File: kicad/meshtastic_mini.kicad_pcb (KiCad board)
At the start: 2 copper layers, 88 x 84 mm, 128 parts, among them U1 ESP32-C3_SuperMini, U10 RFM95W-868S2, U11 ESP32-C3_SuperMini, U12 RFM95W-868S2, U13 ESP32-C3_SuperMini, U14 RFM95W-868S2, U15 ESP32-C3_SuperMini, U16 RFM95W-868S2, U17 ESP32-C3_SuperMini, U18 RFM95W-868S2, U19 ESP32-C3_SuperMini, U2 RFM95W-868S2, U20 RFM95W-868S2, U21 ESP32-C3_SuperMini, U22 RFM95W-868S2, U23 ESP32-C3_SuperMini, U24 RFM95W-868S2, U25 ESP32-C3_SuperMini, U26 RFM95W-868S2, U27 ESP32-C3_SuperMini, U28 RFM95W-868S2, U29 ESP32-C3_SuperMini, U3 ESP32-C3_SuperMini, U30 RFM95W-868S2, U31 ESP32-C3_SuperMini, U32 RFM95W-868S2, U4 RFM95W-868S2, U5 ESP32-C3_SuperMini, U6 RFM95W-868S2, U7 ESP32-C3_SuperMini, U8 RFM95W-868S2, U9 ESP32-C3_SuperMini

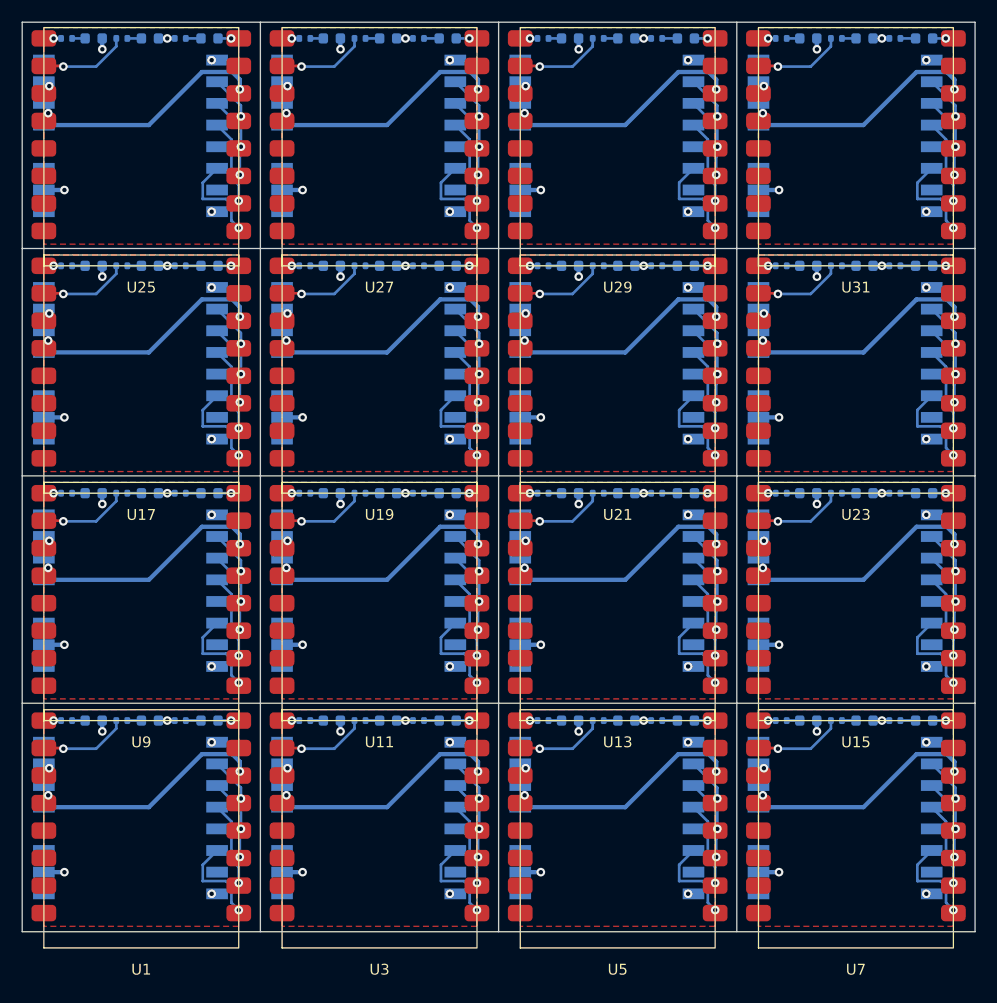
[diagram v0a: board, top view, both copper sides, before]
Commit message: connected DIO0 to pin 10 instead of 9
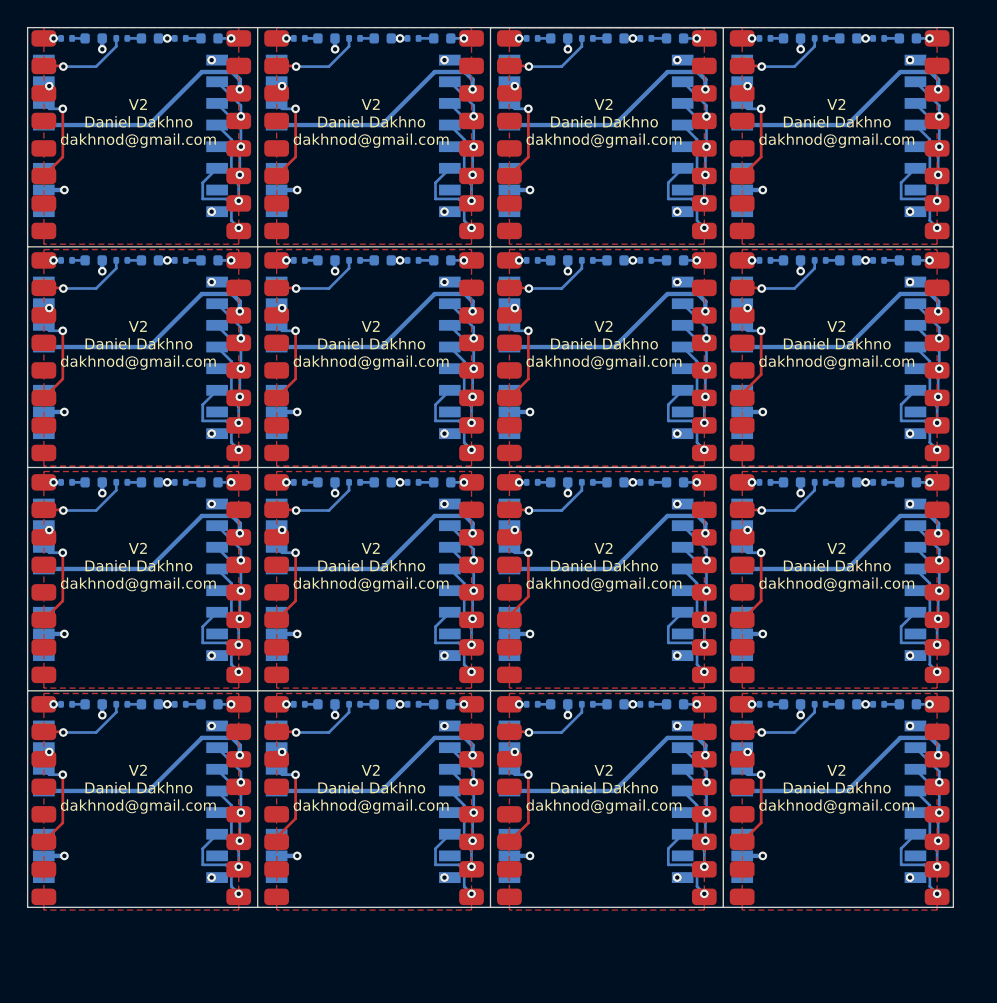
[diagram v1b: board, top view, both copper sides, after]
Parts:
- removed the D1 at (135.6, 103.5)
- removed D10, D11, D12, D13, D14, D15, D16, D17, D18, D19, D20, D21, D22, D23, D24, D25, D26, D27, D28, D29, D30, D31, D32, D33, D34, D35, D36, D4, D40, D41, D42, D43, D44, D45, D46, D47, D48, D5, D6, D7, D8, D9: LED, LED_SMD:LED_0603_1608Metric
- removed the D2 at (140.8, 103.5)
- removed the D3 at (146.3, 103.5)
- removed the R1 at (133.1, 103.5)
- removed R10, R11, R12, R13, R14, R15, R16, R17, R18, R19, R20, R21, R22, R23, R24, R25, R26, R27, R28, R29, R30, R31, R32, R33, R34, R35, R36, R4, R40, R41, R42, R43, R44, R45, R46, R47, R48, R5, R6, R7, R8, R9: 1K, Resistor_SMD:R_0402_1005Metric
- removed the R2 at (138.2, 103.5)
- removed the R3 at (143.6, 103.5)
- removed the U1 at (140.0, 112.5)
- removed U10, U12, U14, U16, U18, U20, U22, U24, U28, U30, U32, U4, U6, U8: RFM95W-868S2, RF_Module:HOPERF_RFM9XW_SMD
- removed U11, U13, U15, U17, U19, U21, U23, U27, U29, U3, U31, U5, U7, U9: ESP32-C3_SuperMini, ESP32:ESP32-C3 SuperMini
- removed the U2 at (139.0, 112.5)
- added D1: LED, LED_SMD:LED_0603_1608Metric, B.Cu at (157.1, 40.5)
- added D1: LED, LED_SMD:LED_0603_1608Metric, B.Cu at (178.6, 61.0)
- added D1: LED, LED_SMD:LED_0603_1608Metric, B.Cu at (200.1, 61.0)
- added D1: LED, LED_SMD:LED_0603_1608Metric, B.Cu at (178.6, 40.5)
- added D1: LED, LED_SMD:LED_0603_1608Metric, B.Cu at (200.1, 40.5)
- added D1: LED, LED_SMD:LED_0603_1608Metric, B.Cu at (135.6, 61.0)
- added D1: LED, LED_SMD:LED_0603_1608Metric, B.Cu at (178.6, 102.0)
- added D1: LED, LED_SMD:LED_0603_1608Metric, B.Cu at (135.6, 81.5)
- added D1: LED, LED_SMD:LED_0603_1608Metric, B.Cu at (178.6, 81.5)
- added D1: LED, LED_SMD:LED_0603_1608Metric, B.Cu at (135.6, 102.0)
- added D1: LED, LED_SMD:LED_0603_1608Metric, B.Cu at (157.1, 61.0)
- added D1: LED, LED_SMD:LED_0603_1608Metric, B.Cu at (157.1, 81.5)
- added D1: LED, LED_SMD:LED_0603_1608Metric, B.Cu at (200.1, 102.0)
- added D1: LED, LED_SMD:LED_0603_1608Metric, B.Cu at (200.1, 81.5)
- added D1: LED, LED_SMD:LED_0603_1608Metric, B.Cu at (157.1, 102.0)
- added D2: LED, LED_SMD:LED_0603_1608Metric, B.Cu at (162.3, 40.5)
- added D2: LED, LED_SMD:LED_0603_1608Metric, B.Cu at (205.3, 81.5)
- added D2: LED, LED_SMD:LED_0603_1608Metric, B.Cu at (140.8, 102.0)
- added D2: LED, LED_SMD:LED_0603_1608Metric, B.Cu at (140.8, 81.5)
- added D2: LED, LED_SMD:LED_0603_1608Metric, B.Cu at (162.3, 81.5)
- added D2: LED, LED_SMD:LED_0603_1608Metric, B.Cu at (183.8, 102.0)
- added D2: LED, LED_SMD:LED_0603_1608Metric, B.Cu at (183.8, 40.5)
- added D2: LED, LED_SMD:LED_0603_1608Metric, B.Cu at (205.3, 40.5)
- added D2: LED, LED_SMD:LED_0603_1608Metric, B.Cu at (183.8, 81.5)
- added D2: LED, LED_SMD:LED_0603_1608Metric, B.Cu at (162.3, 61.0)
- added D2: LED, LED_SMD:LED_0603_1608Metric, B.Cu at (140.8, 61.0)
- added D2: LED, LED_SMD:LED_0603_1608Metric, B.Cu at (205.3, 61.0)
- added D2: LED, LED_SMD:LED_0603_1608Metric, B.Cu at (205.3, 102.0)
- added D2: LED, LED_SMD:LED_0603_1608Metric, B.Cu at (162.3, 102.0)
- added D2: LED, LED_SMD:LED_0603_1608Metric, B.Cu at (183.8, 61.0)
- added D3: LED, LED_SMD:LED_0603_1608Metric, B.Cu at (167.8, 61.0)
- added D3: LED, LED_SMD:LED_0603_1608Metric, B.Cu at (210.8, 40.5)
- added D3: LED, LED_SMD:LED_0603_1608Metric, B.Cu at (210.8, 81.5)
- added D3: LED, LED_SMD:LED_0603_1608Metric, B.Cu at (167.8, 102.0)
- added D3: LED, LED_SMD:LED_0603_1608Metric, B.Cu at (167.8, 40.5)
- added D3: LED, LED_SMD:LED_0603_1608Metric, B.Cu at (189.3, 40.5)
- added D3: LED, LED_SMD:LED_0603_1608Metric, B.Cu at (189.3, 102.0)
- added D3: LED, LED_SMD:LED_0603_1608Metric, B.Cu at (146.3, 81.5)
- added D3: LED, LED_SMD:LED_0603_1608Metric, B.Cu at (189.3, 81.5)
- added D3: LED, LED_SMD:LED_0603_1608Metric, B.Cu at (189.3, 61.0)
- added D3: LED, LED_SMD:LED_0603_1608Metric, B.Cu at (146.3, 102.0)
- added D3: LED, LED_SMD:LED_0603_1608Metric, B.Cu at (210.8, 61.0)
- added D3: LED, LED_SMD:LED_0603_1608Metric, B.Cu at (167.8, 81.5)
- added D3: LED, LED_SMD:LED_0603_1608Metric, B.Cu at (146.3, 61.0)
- added D3: LED, LED_SMD:LED_0603_1608Metric, B.Cu at (210.8, 102.0)
- added R1: 1K, Resistor_SMD:R_0402_1005Metric, B.Cu at (176.1, 81.5)
- added R1: 1K, Resistor_SMD:R_0402_1005Metric, B.Cu at (197.6, 81.5)
- added R1: 1K, Resistor_SMD:R_0402_1005Metric, B.Cu at (133.1, 81.5)
- added R1: 1K, Resistor_SMD:R_0402_1005Metric, B.Cu at (176.1, 61.0)
- added R1: 1K, Resistor_SMD:R_0402_1005Metric, B.Cu at (197.6, 61.0)
- added R1: 1K, Resistor_SMD:R_0402_1005Metric, B.Cu at (197.6, 102.0)
- added R1: 1K, Resistor_SMD:R_0402_1005Metric, B.Cu at (154.6, 102.0)
- added R1: 1K, Resistor_SMD:R_0402_1005Metric, B.Cu at (154.6, 61.0)
- added R1: 1K, Resistor_SMD:R_0402_1005Metric, B.Cu at (197.6, 40.5)
- added R1: 1K, Resistor_SMD:R_0402_1005Metric, B.Cu at (176.1, 40.5)
- added R1: 1K, Resistor_SMD:R_0402_1005Metric, B.Cu at (133.1, 102.0)
- added R1: 1K, Resistor_SMD:R_0402_1005Metric, B.Cu at (133.1, 61.0)
- added R1: 1K, Resistor_SMD:R_0402_1005Metric, B.Cu at (154.6, 40.5)
- added R1: 1K, Resistor_SMD:R_0402_1005Metric, B.Cu at (154.6, 81.5)
- added R1: 1K, Resistor_SMD:R_0402_1005Metric, B.Cu at (176.1, 102.0)
- added R2: 1K, Resistor_SMD:R_0402_1005Metric, B.Cu at (202.7, 81.5)
- added R2: 1K, Resistor_SMD:R_0402_1005Metric, B.Cu at (138.2, 102.0)
- added R2: 1K, Resistor_SMD:R_0402_1005Metric, B.Cu at (159.7, 40.5)
- added R2: 1K, Resistor_SMD:R_0402_1005Metric, B.Cu at (181.2, 40.5)
- added R2: 1K, Resistor_SMD:R_0402_1005Metric, B.Cu at (202.7, 40.5)
- added R2: 1K, Resistor_SMD:R_0402_1005Metric, B.Cu at (159.7, 81.5)
- added R2: 1K, Resistor_SMD:R_0402_1005Metric, B.Cu at (138.2, 61.0)
- added R2: 1K, Resistor_SMD:R_0402_1005Metric, B.Cu at (159.7, 102.0)
- added R2: 1K, Resistor_SMD:R_0402_1005Metric, B.Cu at (202.7, 61.0)
- added R2: 1K, Resistor_SMD:R_0402_1005Metric, B.Cu at (138.2, 81.5)
- added R2: 1K, Resistor_SMD:R_0402_1005Metric, B.Cu at (181.2, 102.0)
- added R2: 1K, Resistor_SMD:R_0402_1005Metric, B.Cu at (202.7, 102.0)
- added R2: 1K, Resistor_SMD:R_0402_1005Metric, B.Cu at (181.2, 61.0)
- added R2: 1K, Resistor_SMD:R_0402_1005Metric, B.Cu at (181.2, 81.5)
- added R2: 1K, Resistor_SMD:R_0402_1005Metric, B.Cu at (159.7, 61.0)
- added R3: 1K, Resistor_SMD:R_0402_1005Metric, B.Cu at (208.1, 102.0)
- added R3: 1K, Resistor_SMD:R_0402_1005Metric, B.Cu at (143.6, 61.0)
- added R3: 1K, Resistor_SMD:R_0402_1005Metric, B.Cu at (165.1, 102.0)
- added R3: 1K, Resistor_SMD:R_0402_1005Metric, B.Cu at (208.1, 61.0)
- added R3: 1K, Resistor_SMD:R_0402_1005Metric, B.Cu at (186.6, 81.5)
- added R3: 1K, Resistor_SMD:R_0402_1005Metric, B.Cu at (143.6, 81.5)
- added R3: 1K, Resistor_SMD:R_0402_1005Metric, B.Cu at (165.1, 61.0)
- added R3: 1K, Resistor_SMD:R_0402_1005Metric, B.Cu at (165.1, 81.5)
- added R3: 1K, Resistor_SMD:R_0402_1005Metric, B.Cu at (165.1, 40.5)
- added R3: 1K, Resistor_SMD:R_0402_1005Metric, B.Cu at (186.6, 102.0)
- added R3: 1K, Resistor_SMD:R_0402_1005Metric, B.Cu at (208.1, 81.5)
- added R3: 1K, Resistor_SMD:R_0402_1005Metric, B.Cu at (186.6, 61.0)
- added R3: 1K, Resistor_SMD:R_0402_1005Metric, B.Cu at (143.6, 102.0)
- added R3: 1K, Resistor_SMD:R_0402_1005Metric, B.Cu at (208.1, 40.5)
- added R3: 1K, Resistor_SMD:R_0402_1005Metric, B.Cu at (186.6, 40.5)
- added U1: ESP32-C3_SuperMini, ESP32:ESP32-C3 SuperMini, F.Cu at (161.5, 70.0)
- added U1: ESP32-C3_SuperMini, ESP32:ESP32-C3 SuperMini, F.Cu at (140.0, 70.0)
- added U1: ESP32-C3_SuperMini, ESP32:ESP32-C3 SuperMini, F.Cu at (161.5, 111.0)
- added U1: ESP32-C3_SuperMini, ESP32:ESP32-C3 SuperMini, F.Cu at (183.0, 70.0)
- added U1: ESP32-C3_SuperMini, ESP32:ESP32-C3 SuperMini, F.Cu at (204.5, 111.0)
- added U1: ESP32-C3_SuperMini, ESP32:ESP32-C3 SuperMini, F.Cu at (204.5, 49.5)
- added U1: ESP32-C3_SuperMini, ESP32:ESP32-C3 SuperMini, F.Cu at (140.0, 111.0)
- added U1: ESP32-C3_SuperMini, ESP32:ESP32-C3 SuperMini, F.Cu at (204.5, 70.0)
- added U1: ESP32-C3_SuperMini, ESP32:ESP32-C3 SuperMini, F.Cu at (183.0, 49.5)
- added U1: ESP32-C3_SuperMini, ESP32:ESP32-C3 SuperMini, F.Cu at (183.0, 90.5)
- added U1: ESP32-C3_SuperMini, ESP32:ESP32-C3 SuperMini, F.Cu at (161.5, 90.5)
- added U1: ESP32-C3_SuperMini, ESP32:ESP32-C3 SuperMini, F.Cu at (183.0, 111.0)
- added U1: ESP32-C3_SuperMini, ESP32:ESP32-C3 SuperMini, F.Cu at (204.5, 90.5)
- added U1: ESP32-C3_SuperMini, ESP32:ESP32-C3 SuperMini, F.Cu at (161.5, 49.5)
- added U1: ESP32-C3_SuperMini, ESP32:ESP32-C3 SuperMini, F.Cu at (140.0, 90.5)
- added U2: RFM95W-868S2, RF_Module:HOPERF_RFM9XW_SMD, B.Cu at (139.0, 70.0)
- added U2: RFM95W-868S2, RF_Module:HOPERF_RFM9XW_SMD, B.Cu at (139.0, 90.5)
- added U2: RFM95W-868S2, RF_Module:HOPERF_RFM9XW_SMD, B.Cu at (182.0, 90.5)
- added U2: RFM95W-868S2, RF_Module:HOPERF_RFM9XW_SMD, B.Cu at (139.0, 111.0)
- added U2: RFM95W-868S2, RF_Module:HOPERF_RFM9XW_SMD, B.Cu at (182.0, 111.0)
- added U2: RFM95W-868S2, RF_Module:HOPERF_RFM9XW_SMD, B.Cu at (160.5, 49.5)
- added U2: RFM95W-868S2, RF_Module:HOPERF_RFM9XW_SMD, B.Cu at (182.0, 70.0)
- added U2: RFM95W-868S2, RF_Module:HOPERF_RFM9XW_SMD, B.Cu at (203.5, 90.5)
- added U2: RFM95W-868S2, RF_Module:HOPERF_RFM9XW_SMD, B.Cu at (160.5, 111.0)
- added U2: RFM95W-868S2, RF_Module:HOPERF_RFM9XW_SMD, B.Cu at (182.0, 49.5)
- added U2: RFM95W-868S2, RF_Module:HOPERF_RFM9XW_SMD, B.Cu at (203.5, 49.5)
- added U2: RFM95W-868S2, RF_Module:HOPERF_RFM9XW_SMD, B.Cu at (203.5, 70.0)
- added U2: RFM95W-868S2, RF_Module:HOPERF_RFM9XW_SMD, B.Cu at (160.5, 90.5)
- added U2: RFM95W-868S2, RF_Module:HOPERF_RFM9XW_SMD, B.Cu at (160.5, 70.0)
- added U2: RFM95W-868S2, RF_Module:HOPERF_RFM9XW_SMD, B.Cu at (203.5, 111.0)
- renumbered D37 to D1, D38 to D2, D39 to D3, R37 to R1, R38 to R2, R39 to R3, U25 to U1, U26 to U2
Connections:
- U1 pad 4: /DIO0 -> unconnected-(U1-Pad4)
- U1 pad 6: unconnected-(U1-Pad6) -> /DIO0
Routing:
- net /DIO0: track 17.1 -> 151.2 mm
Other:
- board size 88 x 84 mm -> 85.5 x 81.2 mm
- board text added: "V2 Daniel Dakhno dakhnod@gmail.com"

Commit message: fixed third LED wiring (that noone will probably ever use)
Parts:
- removed the D1 at (157.1, 40.5)
- removed the D1 at (178.6, 61.0)
- removed the D1 at (200.1, 61.0)
- removed the D1 at (178.6, 40.5)
- removed the D1 at (200.1, 40.5)
- removed the D1 at (135.6, 61.0)
- removed the D1 at (178.6, 102.0)
- removed the D1 at (135.6, 81.5)
- removed the D1 at (178.6, 81.5)
- removed the D1 at (135.6, 102.0)
- removed the D1 at (157.1, 61.0)
- removed the D1 at (157.1, 81.5)
- removed the D1 at (200.1, 102.0)
- removed the D1 at (200.1, 81.5)
- removed the D1 at (157.1, 102.0)
- removed the D2 at (162.3, 40.5)
- removed the D2 at (205.3, 81.5)
- removed the D2 at (140.8, 102.0)
- removed the D2 at (140.8, 81.5)
- removed the D2 at (162.3, 81.5)
- removed the D2 at (183.8, 102.0)
- removed the D2 at (183.8, 40.5)
- removed the D2 at (205.3, 40.5)
- removed the D2 at (183.8, 81.5)
- removed the D2 at (162.3, 61.0)
- removed the D2 at (140.8, 61.0)
- removed the D2 at (205.3, 61.0)
- removed the D2 at (205.3, 102.0)
- removed the D2 at (162.3, 102.0)
- removed the D2 at (183.8, 61.0)
- removed the D3 at (167.8, 61.0)
- removed the D3 at (210.8, 40.5)
- removed the D3 at (210.8, 81.5)
- removed the D3 at (167.8, 102.0)
- removed the D3 at (167.8, 40.5)
- removed the D3 at (189.3, 40.5)
- removed the D3 at (189.3, 102.0)
- removed the D3 at (146.3, 81.5)
- removed the D3 at (189.3, 81.5)
- removed the D3 at (189.3, 61.0)
- removed the D3 at (146.3, 102.0)
- removed the D3 at (210.8, 61.0)
- removed the D3 at (167.8, 81.5)
- removed the D3 at (146.3, 61.0)
- removed the D3 at (210.8, 102.0)
- removed the R1 at (176.1, 81.5)
- removed the R1 at (197.6, 81.5)
- removed the R1 at (133.1, 81.5)
- removed the R1 at (176.1, 61.0)
- removed the R1 at (197.6, 61.0)
- removed the R1 at (197.6, 102.0)
- removed the R1 at (154.6, 102.0)
- removed the R1 at (154.6, 61.0)
- removed the R1 at (197.6, 40.5)
- removed the R1 at (176.1, 40.5)
- removed the R1 at (133.1, 102.0)
- removed the R1 at (133.1, 61.0)
- removed the R1 at (154.6, 40.5)
- removed the R1 at (154.6, 81.5)
- removed the R1 at (176.1, 102.0)
- removed the R2 at (202.7, 81.5)
- removed the R2 at (138.2, 102.0)
- removed the R2 at (159.7, 40.5)
- removed the R2 at (181.2, 40.5)
- removed the R2 at (202.7, 40.5)
- removed the R2 at (159.7, 81.5)
- removed the R2 at (138.2, 61.0)
- removed the R2 at (159.7, 102.0)
- removed the R2 at (202.7, 61.0)
- removed the R2 at (138.2, 81.5)
- removed the R2 at (181.2, 102.0)
- removed the R2 at (202.7, 102.0)
- removed the R2 at (181.2, 61.0)
- removed the R2 at (181.2, 81.5)
- removed the R2 at (159.7, 61.0)
- removed the R3 at (208.1, 102.0)
- removed the R3 at (143.6, 61.0)
- removed the R3 at (165.1, 102.0)
- removed the R3 at (208.1, 61.0)
- removed the R3 at (186.6, 81.5)
- removed the R3 at (143.6, 81.5)
- removed the R3 at (165.1, 61.0)
- removed the R3 at (165.1, 81.5)
- removed the R3 at (165.1, 40.5)
- removed the R3 at (186.6, 102.0)
- removed the R3 at (208.1, 81.5)
- removed the R3 at (186.6, 61.0)
- removed the R3 at (143.6, 102.0)
- removed the R3 at (208.1, 40.5)
- removed the R3 at (186.6, 40.5)
- removed the U1 at (161.5, 70.0)
- removed the U1 at (140.0, 70.0)
- removed the U1 at (161.5, 111.0)
- removed the U1 at (183.0, 70.0)
- removed the U1 at (204.5, 111.0)
- removed the U1 at (204.5, 49.5)
- removed the U1 at (140.0, 111.0)
- removed the U1 at (204.5, 70.0)
- removed the U1 at (183.0, 49.5)
- removed the U1 at (183.0, 90.5)
- removed the U1 at (161.5, 90.5)
- removed the U1 at (183.0, 111.0)
- removed the U1 at (204.5, 90.5)
- removed the U1 at (161.5, 49.5)
- removed the U1 at (140.0, 90.5)
- removed the U2 at (139.0, 70.0)
- removed the U2 at (139.0, 90.5)
- removed the U2 at (182.0, 90.5)
- removed the U2 at (139.0, 111.0)
- removed the U2 at (182.0, 111.0)
- removed the U2 at (160.5, 49.5)
- removed the U2 at (182.0, 70.0)
- removed the U2 at (203.5, 90.5)
- removed the U2 at (160.5, 111.0)
- removed the U2 at (182.0, 49.5)
- removed the U2 at (203.5, 49.5)
- removed the U2 at (203.5, 70.0)
- removed the U2 at (160.5, 90.5)
- removed the U2 at (160.5, 70.0)
- removed the U2 at (203.5, 111.0)
- added D10: LED, LED_SMD:LED_0603_1608Metric, B.Cu at (178.6, 40.5)
- added D11: LED, LED_SMD:LED_0603_1608Metric, B.Cu at (183.8, 40.5)
- added D12: LED, LED_SMD:LED_0603_1608Metric, B.Cu at (189.3, 40.5)
- added D13: LED, LED_SMD:LED_0603_1608Metric, B.Cu at (200.1, 40.5)
- added D14: LED, LED_SMD:LED_0603_1608Metric, B.Cu at (205.3, 40.5)
- added D15: LED, LED_SMD:LED_0603_1608Metric, B.Cu at (210.8, 40.5)
- added D16: LED, LED_SMD:LED_0603_1608Metric, B.Cu at (135.6, 61.0)
- added D17: LED, LED_SMD:LED_0603_1608Metric, B.Cu at (140.8, 61.0)
- added D18: LED, LED_SMD:LED_0603_1608Metric, B.Cu at (146.3, 61.0)
- added D19: LED, LED_SMD:LED_0603_1608Metric, B.Cu at (157.1, 61.0)
- added D20: LED, LED_SMD:LED_0603_1608Metric, B.Cu at (162.3, 61.0)
- added D21: LED, LED_SMD:LED_0603_1608Metric, B.Cu at (167.8, 61.0)
- added D22: LED, LED_SMD:LED_0603_1608Metric, B.Cu at (178.6, 61.0)
- added D23: LED, LED_SMD:LED_0603_1608Metric, B.Cu at (183.8, 61.0)
- added D24: LED, LED_SMD:LED_0603_1608Metric, B.Cu at (189.3, 61.0)
- added D25: LED, LED_SMD:LED_0603_1608Metric, B.Cu at (200.1, 61.0)
- added D26: LED, LED_SMD:LED_0603_1608Metric, B.Cu at (205.3, 61.0)
- added D27: LED, LED_SMD:LED_0603_1608Metric, B.Cu at (210.8, 61.0)
- added D28: LED, LED_SMD:LED_0603_1608Metric, B.Cu at (135.6, 81.5)
- added D29: LED, LED_SMD:LED_0603_1608Metric, B.Cu at (140.8, 81.5)
- added D30: LED, LED_SMD:LED_0603_1608Metric, B.Cu at (146.3, 81.5)
- added D31: LED, LED_SMD:LED_0603_1608Metric, B.Cu at (157.1, 81.5)
- added D32: LED, LED_SMD:LED_0603_1608Metric, B.Cu at (162.3, 81.5)
- added D33: LED, LED_SMD:LED_0603_1608Metric, B.Cu at (167.8, 81.5)
- added D34: LED, LED_SMD:LED_0603_1608Metric, B.Cu at (178.6, 81.5)
- added D35: LED, LED_SMD:LED_0603_1608Metric, B.Cu at (183.8, 81.5)
- added D36: LED, LED_SMD:LED_0603_1608Metric, B.Cu at (189.3, 81.5)
- added D37: LED, LED_SMD:LED_0603_1608Metric, B.Cu at (200.1, 81.5)
- added D38: LED, LED_SMD:LED_0603_1608Metric, B.Cu at (205.3, 81.5)
- added D39: LED, LED_SMD:LED_0603_1608Metric, B.Cu at (210.8, 81.5)
- added D4: LED, LED_SMD:LED_0603_1608Metric, B.Cu at (135.6, 40.5)
- added D40: LED, LED_SMD:LED_0603_1608Metric, B.Cu at (135.6, 102.0)
- added D41: LED, LED_SMD:LED_0603_1608Metric, B.Cu at (140.8, 102.0)
- added D42: LED, LED_SMD:LED_0603_1608Metric, B.Cu at (146.3, 102.0)
- added D43: LED, LED_SMD:LED_0603_1608Metric, B.Cu at (157.1, 102.0)
- added D44: LED, LED_SMD:LED_0603_1608Metric, B.Cu at (162.3, 102.0)
- added D45: LED, LED_SMD:LED_0603_1608Metric, B.Cu at (167.8, 102.0)
- added D46: LED, LED_SMD:LED_0603_1608Metric, B.Cu at (178.6, 102.0)
- added D47: LED, LED_SMD:LED_0603_1608Metric, B.Cu at (183.8, 102.0)
- added D48: LED, LED_SMD:LED_0603_1608Metric, B.Cu at (189.3, 102.0)
- added D5: LED, LED_SMD:LED_0603_1608Metric, B.Cu at (140.8, 40.5)
- added D6: LED, LED_SMD:LED_0603_1608Metric, B.Cu at (146.3, 40.5)
- added D7: LED, LED_SMD:LED_0603_1608Metric, B.Cu at (157.1, 40.5)
- added D8: LED, LED_SMD:LED_0603_1608Metric, B.Cu at (162.3, 40.5)
- added D9: LED, LED_SMD:LED_0603_1608Metric, B.Cu at (167.8, 40.5)
- added R10: 1K, Resistor_SMD:R_0402_1005Metric, B.Cu at (176.1, 40.5)
- added R11: 1K, Resistor_SMD:R_0402_1005Metric, B.Cu at (181.2, 40.5)
- added R12: 1K, Resistor_SMD:R_0402_1005Metric, B.Cu at (186.6, 40.5)
- added R13: 1K, Resistor_SMD:R_0402_1005Metric, B.Cu at (197.6, 40.5)
- added R14: 1K, Resistor_SMD:R_0402_1005Metric, B.Cu at (202.7, 40.5)
- added R15: 1K, Resistor_SMD:R_0402_1005Metric, B.Cu at (208.1, 40.5)
- added R16: 1K, Resistor_SMD:R_0402_1005Metric, B.Cu at (133.1, 61.0)
- added R17: 1K, Resistor_SMD:R_0402_1005Metric, B.Cu at (138.2, 61.0)
- added R18: 1K, Resistor_SMD:R_0402_1005Metric, B.Cu at (143.6, 61.0)
- added R19: 1K, Resistor_SMD:R_0402_1005Metric, B.Cu at (154.6, 61.0)
- added R20: 1K, Resistor_SMD:R_0402_1005Metric, B.Cu at (159.7, 61.0)
- added R21: 1K, Resistor_SMD:R_0402_1005Metric, B.Cu at (165.1, 61.0)
- added R22: 1K, Resistor_SMD:R_0402_1005Metric, B.Cu at (176.1, 61.0)
- added R23: 1K, Resistor_SMD:R_0402_1005Metric, B.Cu at (181.2, 61.0)
- added R24: 1K, Resistor_SMD:R_0402_1005Metric, B.Cu at (186.6, 61.0)
- added R25: 1K, Resistor_SMD:R_0402_1005Metric, B.Cu at (197.6, 61.0)
- added R26: 1K, Resistor_SMD:R_0402_1005Metric, B.Cu at (202.7, 61.0)
- added R27: 1K, Resistor_SMD:R_0402_1005Metric, B.Cu at (208.1, 61.0)
- added R28: 1K, Resistor_SMD:R_0402_1005Metric, B.Cu at (133.1, 81.5)
- added R29: 1K, Resistor_SMD:R_0402_1005Metric, B.Cu at (138.2, 81.5)
- added R30: 1K, Resistor_SMD:R_0402_1005Metric, B.Cu at (143.6, 81.5)
- added R31: 1K, Resistor_SMD:R_0402_1005Metric, B.Cu at (154.6, 81.5)
- added R32: 1K, Resistor_SMD:R_0402_1005Metric, B.Cu at (159.7, 81.5)
- added R33: 1K, Resistor_SMD:R_0402_1005Metric, B.Cu at (165.1, 81.5)
- added R34: 1K, Resistor_SMD:R_0402_1005Metric, B.Cu at (176.1, 81.5)
- added R35: 1K, Resistor_SMD:R_0402_1005Metric, B.Cu at (181.2, 81.5)
- added R36: 1K, Resistor_SMD:R_0402_1005Metric, B.Cu at (186.6, 81.5)
- added R37: 1K, Resistor_SMD:R_0402_1005Metric, B.Cu at (197.6, 81.5)
- added R38: 1K, Resistor_SMD:R_0402_1005Metric, B.Cu at (202.7, 81.5)
- added R39: 1K, Resistor_SMD:R_0402_1005Metric, B.Cu at (208.1, 81.5)
- added R4: 1K, Resistor_SMD:R_0402_1005Metric, B.Cu at (133.1, 40.5)
- added R40: 1K, Resistor_SMD:R_0402_1005Metric, B.Cu at (133.1, 102.0)
- added R41: 1K, Resistor_SMD:R_0402_1005Metric, B.Cu at (138.2, 102.0)
- added R42: 1K, Resistor_SMD:R_0402_1005Metric, B.Cu at (143.6, 102.0)
- added R43: 1K, Resistor_SMD:R_0402_1005Metric, B.Cu at (154.6, 102.0)
- added R44: 1K, Resistor_SMD:R_0402_1005Metric, B.Cu at (159.7, 102.0)
- added R45: 1K, Resistor_SMD:R_0402_1005Metric, B.Cu at (165.1, 102.0)
- added R46: 1K, Resistor_SMD:R_0402_1005Metric, B.Cu at (176.1, 102.0)
- added R47: 1K, Resistor_SMD:R_0402_1005Metric, B.Cu at (181.2, 102.0)
- added R48: 1K, Resistor_SMD:R_0402_1005Metric, B.Cu at (186.6, 102.0)
- added R5: 1K, Resistor_SMD:R_0402_1005Metric, B.Cu at (138.2, 40.5)
- added R6: 1K, Resistor_SMD:R_0402_1005Metric, B.Cu at (143.6, 40.5)
- added R7: 1K, Resistor_SMD:R_0402_1005Metric, B.Cu at (154.6, 40.5)
- added R8: 1K, Resistor_SMD:R_0402_1005Metric, B.Cu at (159.7, 40.5)
- added R9: 1K, Resistor_SMD:R_0402_1005Metric, B.Cu at (165.1, 40.5)
- added U10: RFM95W-868S2, RF_Module:HOPERF_RFM9XW_SMD, B.Cu at (203.5, 49.5)
- added U11: ESP32-C3_SuperMini, ESP32:ESP32-C3 SuperMini, F.Cu at (140.0, 70.0)
- added U12: RFM95W-868S2, RF_Module:HOPERF_RFM9XW_SMD, B.Cu at (139.0, 70.0)
- added U13: ESP32-C3_SuperMini, ESP32:ESP32-C3 SuperMini, F.Cu at (161.5, 70.0)
- added U14: RFM95W-868S2, RF_Module:HOPERF_RFM9XW_SMD, B.Cu at (160.5, 70.0)
- added U15: ESP32-C3_SuperMini, ESP32:ESP32-C3 SuperMini, F.Cu at (183.0, 70.0)
- added U16: RFM95W-868S2, RF_Module:HOPERF_RFM9XW_SMD, B.Cu at (182.0, 70.0)
- added U17: ESP32-C3_SuperMini, ESP32:ESP32-C3 SuperMini, F.Cu at (204.5, 70.0)
- added U18: RFM95W-868S2, RF_Module:HOPERF_RFM9XW_SMD, B.Cu at (203.5, 70.0)
- added U19: ESP32-C3_SuperMini, ESP32:ESP32-C3 SuperMini, F.Cu at (140.0, 90.5)
- added U20: RFM95W-868S2, RF_Module:HOPERF_RFM9XW_SMD, B.Cu at (139.0, 90.5)
- added U21: ESP32-C3_SuperMini, ESP32:ESP32-C3 SuperMini, F.Cu at (161.5, 90.5)
- added U22: RFM95W-868S2, RF_Module:HOPERF_RFM9XW_SMD, B.Cu at (160.5, 90.5)
- added U23: ESP32-C3_SuperMini, ESP32:ESP32-C3 SuperMini, F.Cu at (183.0, 90.5)
- added U24: RFM95W-868S2, RF_Module:HOPERF_RFM9XW_SMD, B.Cu at (182.0, 90.5)
- added U25: ESP32-C3_SuperMini, ESP32:ESP32-C3 SuperMini, F.Cu at (204.5, 90.5)
- added U26: RFM95W-868S2, RF_Module:HOPERF_RFM9XW_SMD, B.Cu at (203.5, 90.5)
- added U27: ESP32-C3_SuperMini, ESP32:ESP32-C3 SuperMini, F.Cu at (140.0, 111.0)
- added U28: RFM95W-868S2, RF_Module:HOPERF_RFM9XW_SMD, B.Cu at (139.0, 111.0)
- added U29: ESP32-C3_SuperMini, ESP32:ESP32-C3 SuperMini, F.Cu at (161.5, 111.0)
- added U3: ESP32-C3_SuperMini, ESP32:ESP32-C3 SuperMini, F.Cu at (140.0, 49.5)
- added U30: RFM95W-868S2, RF_Module:HOPERF_RFM9XW_SMD, B.Cu at (160.5, 111.0)
- added U31: ESP32-C3_SuperMini, ESP32:ESP32-C3 SuperMini, F.Cu at (183.0, 111.0)
- added U32: RFM95W-868S2, RF_Module:HOPERF_RFM9XW_SMD, B.Cu at (182.0, 111.0)
- added U4: RFM95W-868S2, RF_Module:HOPERF_RFM9XW_SMD, B.Cu at (139.0, 49.5)
- added U5: ESP32-C3_SuperMini, ESP32:ESP32-C3 SuperMini, F.Cu at (161.5, 49.5)
- added U6: RFM95W-868S2, RF_Module:HOPERF_RFM9XW_SMD, B.Cu at (160.5, 49.5)
- added U7: ESP32-C3_SuperMini, ESP32:ESP32-C3 SuperMini, F.Cu at (183.0, 49.5)
- added U8: RFM95W-868S2, RF_Module:HOPERF_RFM9XW_SMD, B.Cu at (182.0, 49.5)
- added U9: ESP32-C3_SuperMini, ESP32:ESP32-C3 SuperMini, F.Cu at (204.5, 49.5)
- moved D1 89.1 mm to (200.1, 102.0)
- moved D2 89.1 mm to (205.3, 102.0)
- moved D3 89.1 mm to (210.8, 102.0), turned to 180 degrees
- moved R1 89.1 mm to (197.6, 102.0)
- moved R2 89.1 mm to (202.7, 102.0)
- moved R3 89.1 mm to (208.1, 102.0), turned to 0 degrees
- moved U1 89.1 mm to (204.5, 111.0)
- moved U2 89.1 mm to (203.5, 111.0)
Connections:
- D3 pad 1: Net-(D3-Pad1) -> GND
- D3 pad 2: Net-(D3-Pad2) -> Net-(D3-A)
- R3 pad 1: Net-(D3-Pad1) -> Net-(U1-GPIO20)
- R3 pad 2: GND -> Net-(D3-A)
- U1 pad 7: unconnected-(U1-Pad7) -> Net-(U1-GPIO20)
- U1 pad 9: Net-(D3-Pad2) -> unconnected-(U1-5V-Pad9)
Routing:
- net Net-(U1-GPIO20): track 0.00 -> 354.1 mm, vias 0 -> 16
- net GND: track 70.5 -> 99.0 mm, vias 80 -> 112
- net Net-(D3-Pad1): track 22.4 -> 0.00 mm
- net Net-(D3-A): track 0.00 -> 22.4 mm
- net Net-(D3-Pad2): track 19.4 -> 0.00 mm, vias 16 -> 0
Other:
- board text added: "V2.2 Daniel Dakhno dakhnod@gmail.com"
- board text removed: "V2 Daniel Dakhno dakhnod@gmail.com"

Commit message: adapted for usage with XIAO nrf52 module
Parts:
- removed the D1 at (200.1, 102.0)
- removed the D2 at (205.3, 102.0)
- removed the D3 at (210.8, 102.0)
- removed the R1 at (197.6, 102.0)
- removed the R2 at (202.7, 102.0)
- removed the R3 at (208.1, 102.0)
- removed the U1 at (204.5, 111.0)
- removed the U2 at (203.5, 111.0)
- added D4: LED, LED_SMD:LED_0603_1608Metric, B.Cu at (135.6, 40.5)
- added D5: LED, LED_SMD:LED_0603_1608Metric, B.Cu at (140.8, 40.5)
- added D6: LED, LED_SMD:LED_0603_1608Metric, B.Cu at (146.3, 40.5)
- added R4: 1K, Resistor_SMD:R_0402_1005Metric, B.Cu at (133.1, 40.5)
- added R5: 1K, Resistor_SMD:R_0402_1005Metric, B.Cu at (138.2, 40.5)
- added R6: 1K, Resistor_SMD:R_0402_1005Metric, B.Cu at (143.6, 40.5)
- added U3: ESP32-C3_SuperMini, ESP32:ESP32-C3 SuperMini, F.Cu at (140.0, 49.5)
- added U4: RFM95W-868S2, RF_Module:HOPERF_RFM9XW_SMD, B.Cu at (139.0, 49.5)
- moved D1 89.1 mm to (200.1, 102.0)
- moved D2 89.1 mm to (205.3, 102.0)
- moved D3 89.1 mm to (210.8, 102.0)
- moved R1 89.1 mm to (197.6, 102.0)
- moved R2 89.1 mm to (202.7, 102.0)
- moved R3 89.1 mm to (208.1, 102.0)
- moved U1 89.1 mm to (204.5, 111.0)
- moved U2 89.1 mm to (203.5, 111.0)
- renumbered D4 to D1, D5 to D2, D6 to D3, R4 to R1, R5 to R2, R6 to R3, U3 to U1, U4 to U2
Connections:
- R12 pad 1: Net-(U1-GPIO20) -> Net-(U1-GPIO0)
- R15 pad 1: Net-(U1-GPIO20) -> Net-(U1-GPIO0)
- R18 pad 1: Net-(U1-GPIO20) -> Net-(U1-GPIO0)
- R21 pad 1: Net-(U1-GPIO20) -> Net-(U1-GPIO0)
- R24 pad 1: Net-(U1-GPIO20) -> Net-(U1-GPIO0)
- R27 pad 1: Net-(U1-GPIO20) -> Net-(U1-GPIO0)
- R3 pad 1: Net-(U1-GPIO20) -> Net-(U1-GPIO0)
- R30 pad 1: Net-(U1-GPIO20) -> Net-(U1-GPIO0)
- R33 pad 1: Net-(U1-GPIO20) -> Net-(U1-GPIO0)
- R36 pad 1: Net-(U1-GPIO20) -> Net-(U1-GPIO0)
- R39 pad 1: Net-(U1-GPIO20) -> Net-(U1-GPIO0)
- R42 pad 1: Net-(U1-GPIO20) -> Net-(U1-GPIO0)
- R45 pad 1: Net-(U1-GPIO20) -> Net-(U1-GPIO0)
- R48 pad 1: Net-(U1-GPIO20) -> Net-(U1-GPIO0)
- R9 pad 1: Net-(U1-GPIO20) -> Net-(U1-GPIO0)
- U1 pad 16: /RESET -> Net-(U1-GPIO0)
- U1 pad 7: Net-(U1-GPIO20) -> /RESET
- U11 pad 16: /RESET -> Net-(U1-GPIO0)
- U11 pad 7: Net-(U1-GPIO20) -> /RESET
- U13 pad 16: /RESET -> Net-(U1-GPIO0)
- U13 pad 7: Net-(U1-GPIO20) -> /RESET
- U15 pad 16: /RESET -> Net-(U1-GPIO0)
- U15 pad 7: Net-(U1-GPIO20) -> /RESET
- U17 pad 16: /RESET -> Net-(U1-GPIO0)
- U17 pad 7: Net-(U1-GPIO20) -> /RESET
- U19 pad 16: /RESET -> Net-(U1-GPIO0)
- U19 pad 7: Net-(U1-GPIO20) -> /RESET
- U21 pad 16: /RESET -> Net-(U1-GPIO0)
- U21 pad 7: Net-(U1-GPIO20) -> /RESET
- U23 pad 16: /RESET -> Net-(U1-GPIO0)
- U23 pad 7: Net-(U1-GPIO20) -> /RESET
- U25 pad 16: /RESET -> Net-(U1-GPIO0)
- U25 pad 7: Net-(U1-GPIO20) -> /RESET
- U27 pad 16: /RESET -> Net-(U1-GPIO0)
- U27 pad 7: Net-(U1-GPIO20) -> /RESET
- U29 pad 16: /RESET -> Net-(U1-GPIO0)
- U29 pad 7: Net-(U1-GPIO20) -> /RESET
- U31 pad 16: /RESET -> Net-(U1-GPIO0)
- U31 pad 7: Net-(U1-GPIO20) -> /RESET
- U5 pad 16: /RESET -> Net-(U1-GPIO0)
- U5 pad 7: Net-(U1-GPIO20) -> /RESET
- U7 pad 16: /RESET -> Net-(U1-GPIO0)
- U7 pad 7: Net-(U1-GPIO20) -> /RESET
- U9 pad 16: /RESET -> Net-(U1-GPIO0)
- U9 pad 7: Net-(U1-GPIO20) -> /RESET
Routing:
- net Net-(U1-GPIO20): track 354.1 -> 0.00 mm, vias 16 -> 0
- net Net-(U1-GPIO0): track 0.00 -> 323.6 mm, vias 0 -> 16
- net /RESET: track 139.0 -> 286.4 mm
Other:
- board text added: "V2.3 Daniel Dakhno dakhnod@gmail.com"
- board text removed: "V2.2 Daniel Dakhno dakhnod@gmail.com"
